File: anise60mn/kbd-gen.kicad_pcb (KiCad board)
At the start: 2 copper layers, 284.6 x 94.2 mm, 141 parts, among them CN1 BTB, CN2 BTB, P1 P, P2 P

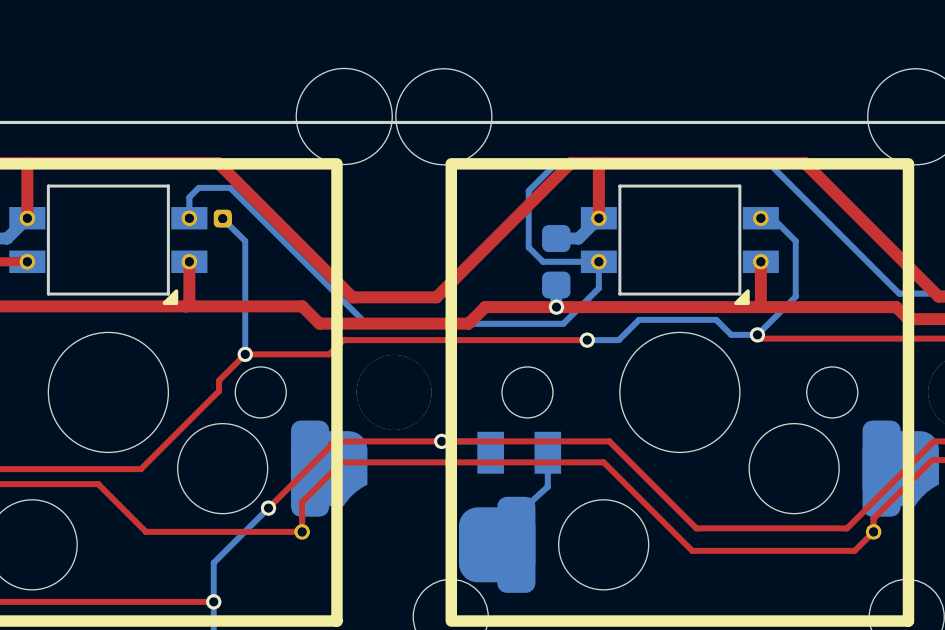
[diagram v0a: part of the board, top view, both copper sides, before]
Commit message: update with anise90 seris/ outline and holes are not fully ready
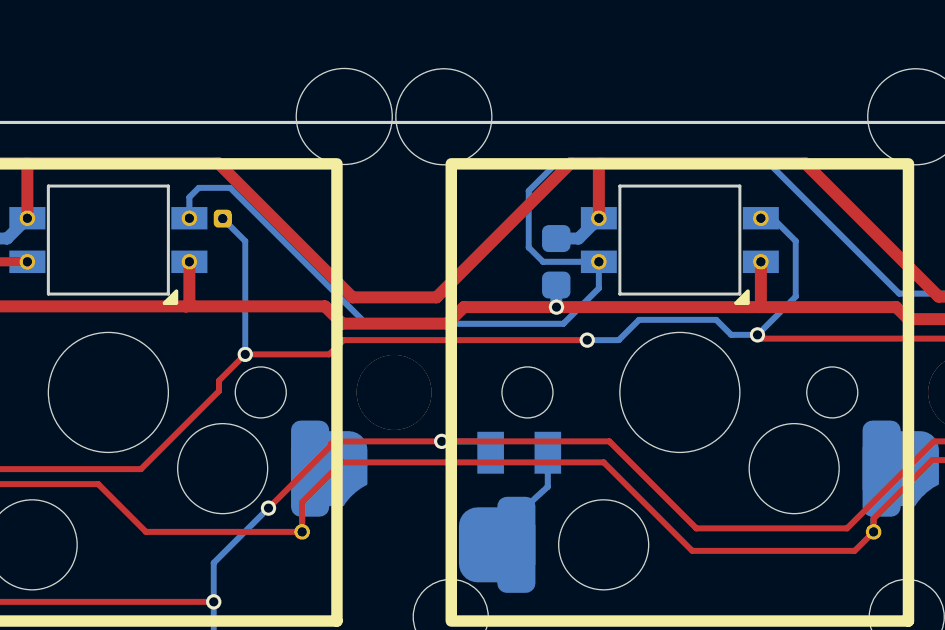
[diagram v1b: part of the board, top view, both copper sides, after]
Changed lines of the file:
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@@
   (segment (start 298 109.15) (end 328.5 109.15) (width 0.4) (layer "F.Cu") (net 3))
   (segment (start 207.375 71) (end 226.525 71) (width 0.4) (layer "F.Cu") (net 3))
-  (segment (start 178.7 71.525) (end 179.25 70.975) (width 0.4) (layer "F.Cu") (net 3))
   (segment (start 322.825 147.175) (end 322.8 147.2) (width 0.4) (layer "F.Cu") (net 3))
   (segment (start 207.4875 128.1375) (end 207.4875 126.61375) (width 0.4) (layer "F.Cu") (net 3))
@@
   (segment (start 72.225 90.3) (end 72.2 90.275) (width 0.4) (layer "F.Cu") (net 3))
   (segment (start 150.3375 69.46375) (end 150.3375 70.9125) (width 0.4) (layer "F.Cu") (net 3))
+  (segment (start 173.91 70.95) (end 174.485 71.525) (width 0.4) (layer "F.Cu") (net 3))
   (segment (start 276.875 147.2) (end 262.25625 147.2) (width 0.4) (layer "F.Cu") (net 3))
   (segment (start 325.275 90.175) (end 335.825 90.175) (width 0.4) (layer "F.Cu") (net 3))
@@
   (segment (start 205.7 147.2) (end 205.625 147.125) (width 0.4) (layer "F.Cu") (net 3))
   (segment (start 321.815 128.175) (end 340.525 128.175) (width 0.4) (layer "F.Cu") (net 3))
-  (segment (start 173.15 70.95) (end 173.725 71.525) (width 0.4) (layer "F.Cu") (net 3))
   (segment (start 302.7375 70.8875) (end 302.625 71) (width 0.4) (layer "F.Cu") (net 3))
   (segment (start 226.55 128.175) (end 226.5375 128.1625) (width 0.4) (layer "F.Cu") (net 3))
@@
   (segment (start 93.1875 69.46375) (end 93.1875 70.8875) (width 0.4) (layer "F.Cu") (net 3))
   (segment (start 302.75 128.175) (end 302.7375 128.1625) (width 0.4) (layer "F.Cu") (net 3))
-  (segment (start 173.725 71.525) (end 178.7 71.525) (width 0.4) (layer "F.Cu") (net 3))
   (segment (start 321.75 147.2) (end 321.7875 147.1625) (width 0.4) (layer "F.Cu") (net 3))
   (segment (start 274.175 90.05) (end 274.1625 90.0375) (width 0.4) (layer "F.Cu") (net 3))
@@
   (segment (start 321.75 147.2) (end 302.8 147.2) (width 0.4) (layer "F.Cu") (net 3))
   (segment (start 81.28125 109.2) (end 74.575 109.2) (width 0.4) (layer "F.Cu") (net 3))
-  (segment (start 169.275 70.95) (end 173.15 70.95) (width 0.4) (layer "F.Cu") (net 3))
   (segment (start 131.2875 70.9375) (end 131.275 70.95) (width 0.4) (layer "F.Cu") (net 3))
   (segment (start 240.825 107.56375) (end 240.825 109.125) (width 0.4) (layer "F.Cu") (net 3))
@@
   (segment (start 187.85 128.175) (end 188.4375 127.5875) (width 0.4) (layer "F.Cu") (net 3))
   (segment (start 259.875 107.56375) (end 259.875 109.125) (width 0.4) (layer "F.Cu") (net 3))
+  (segment (start 174.485 71.525) (end 177.985 71.525) (width 0.4) (layer "F.Cu") (net 3))
   (segment (start 283.6875 69.46375) (end 283.6875 70.9375) (width 0.4) (layer "F.Cu") (net 3))
   (segment (start 264.6375 69.46375) (end 264.6375 70.9625) (width 0.4) (layer "F.Cu") (net 3))
@@
   (segment (start 319.675 81.475) (end 326.875 81.475) (width 0.4) (layer "F.Cu") (net 3))
   (segment (start 112.2 128.175) (end 131.25 128.175) (width 0.4) (layer "F.Cu") (net 3))
+  (segment (start 177.985 71.525) (end 178.535 70.975) (width 0.4) (layer "F.Cu") (net 3))
   (segment (start 293.225 90.05) (end 312.4 90.05) (width 0.4) (layer "F.Cu") (net 3))
   (segment (start 226.5375 128.1625) (end 226.5375 126.61375) (width 0.4) (layer "F.Cu") (net 3))
@@
   (segment (start 112.2 128.175) (end 112.2375 128.1375) (width 0.4) (layer "F.Cu") (net 3))
   (segment (start 207.4875 70.8875) (end 207.375 71) (width 0.3) (layer "F.Cu") (net 3))
-  (segment (start 179.25 70.975) (end 188.375 70.975) (width 0.4) (layer "F.Cu") (net 3))
+  (segment (start 169.275 70.95) (end 173.91 70.95) (width 0.4) (layer "F.Cu") (net 3))
   (segment (start 150.375 128.175) (end 150.3375 128.1375) (width 0.4) (layer "F.Cu") (net 3))
   (segment (start 302.8 147.2) (end 283.7 147.2) (width 0.4) (layer "F.Cu") (net 3))
@@
   (segment (start 340.8375 70.3125) (end 340.8375 69.46375) (width 0.4) (layer "F.Cu") (net 3))
   (segment (start 274.1625 90.0375) (end 274.1625 88.51375) (width 0.4) (layer "F.Cu") (net 3))
+  (segment (start 178.535 70.975) (end 188.375 70.975) (width 0.4) (layer "F.Cu") (net 3))
   (segment (start 81.28125 107.56375) (end 81.28125 109.2) (width 0.4) (layer "F.Cu") (net 3))
   (segment (start 302.8 147.2) (end 302.7375 147.1375) (width 0.4) (layer "F.Cu") (net 3))
